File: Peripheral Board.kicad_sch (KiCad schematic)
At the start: 29 parts, among them J1 JAE_SIM_Card_SF72S006, J10 Conn_01x13_Male, J11 Conn_01x16_Male, J2 524372472, J4 5024268012, U1 MPU-9250, U7 XC6206-2.8V, U8 RT9166-12GVL

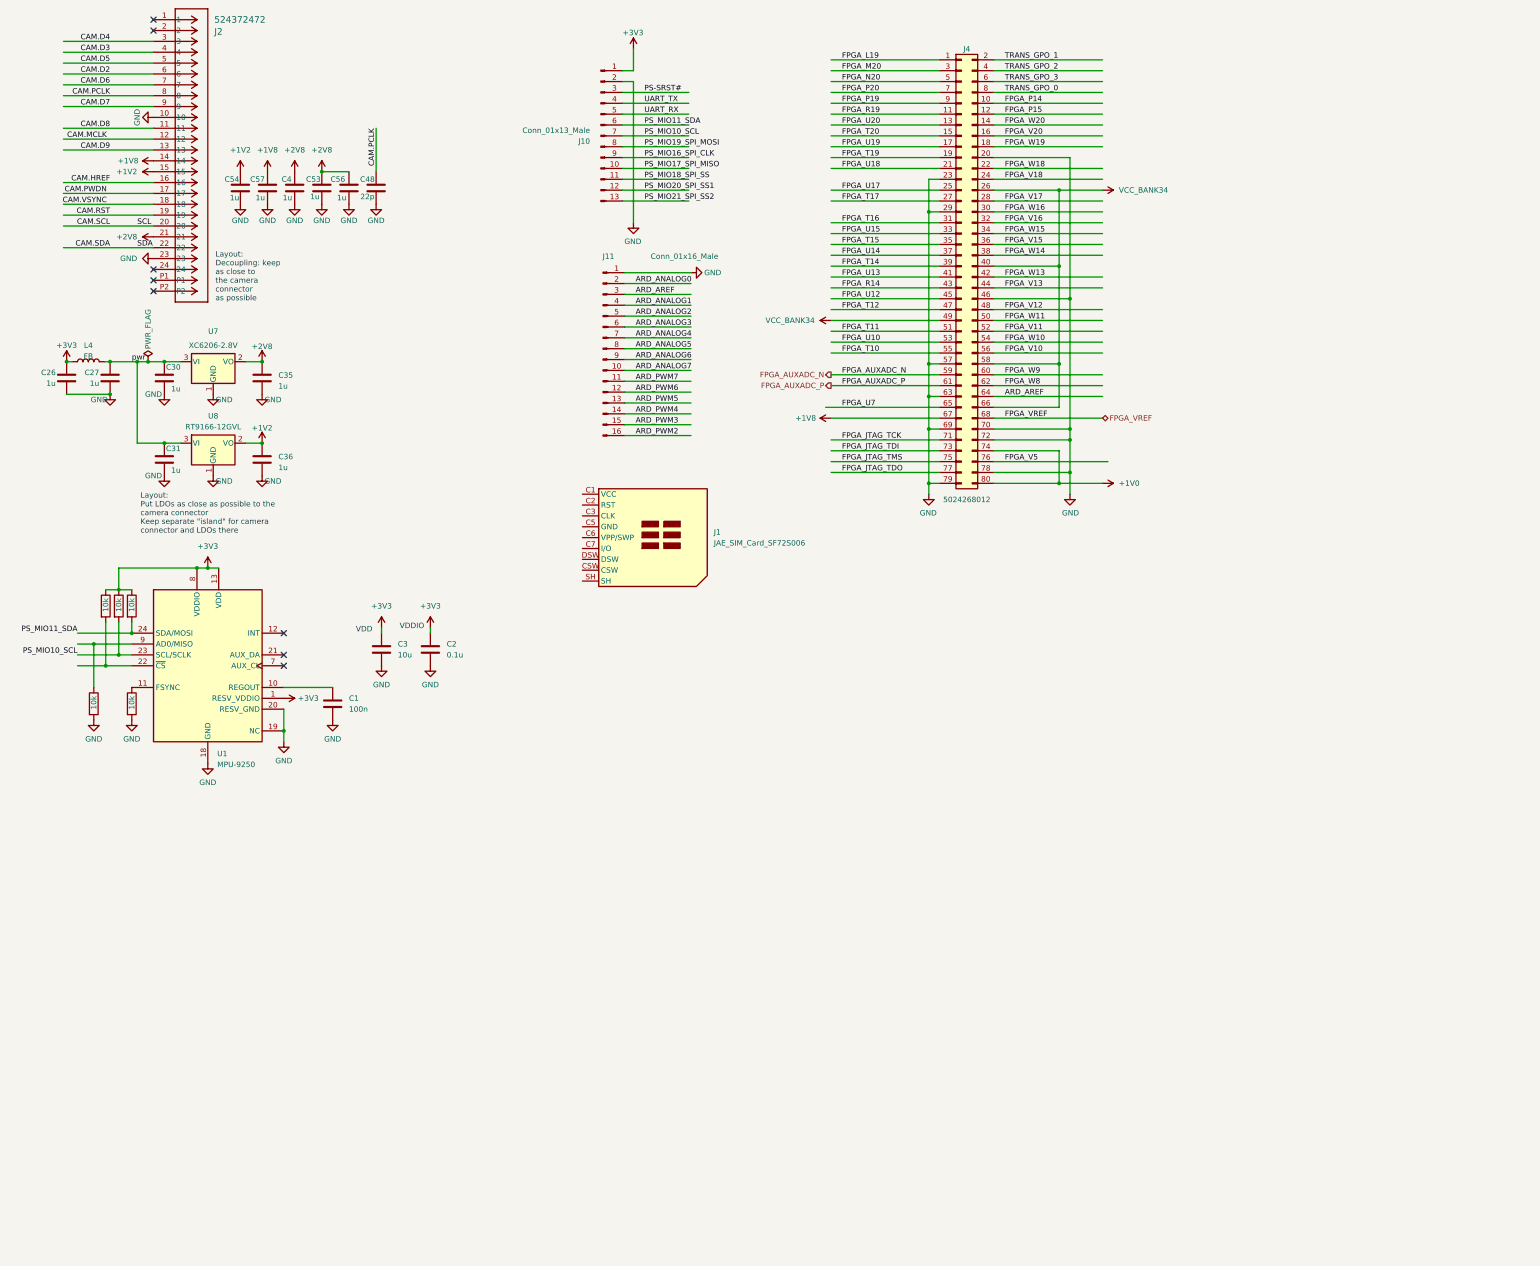
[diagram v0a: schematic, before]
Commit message: Added sd card, routed camera, and added esp32c3
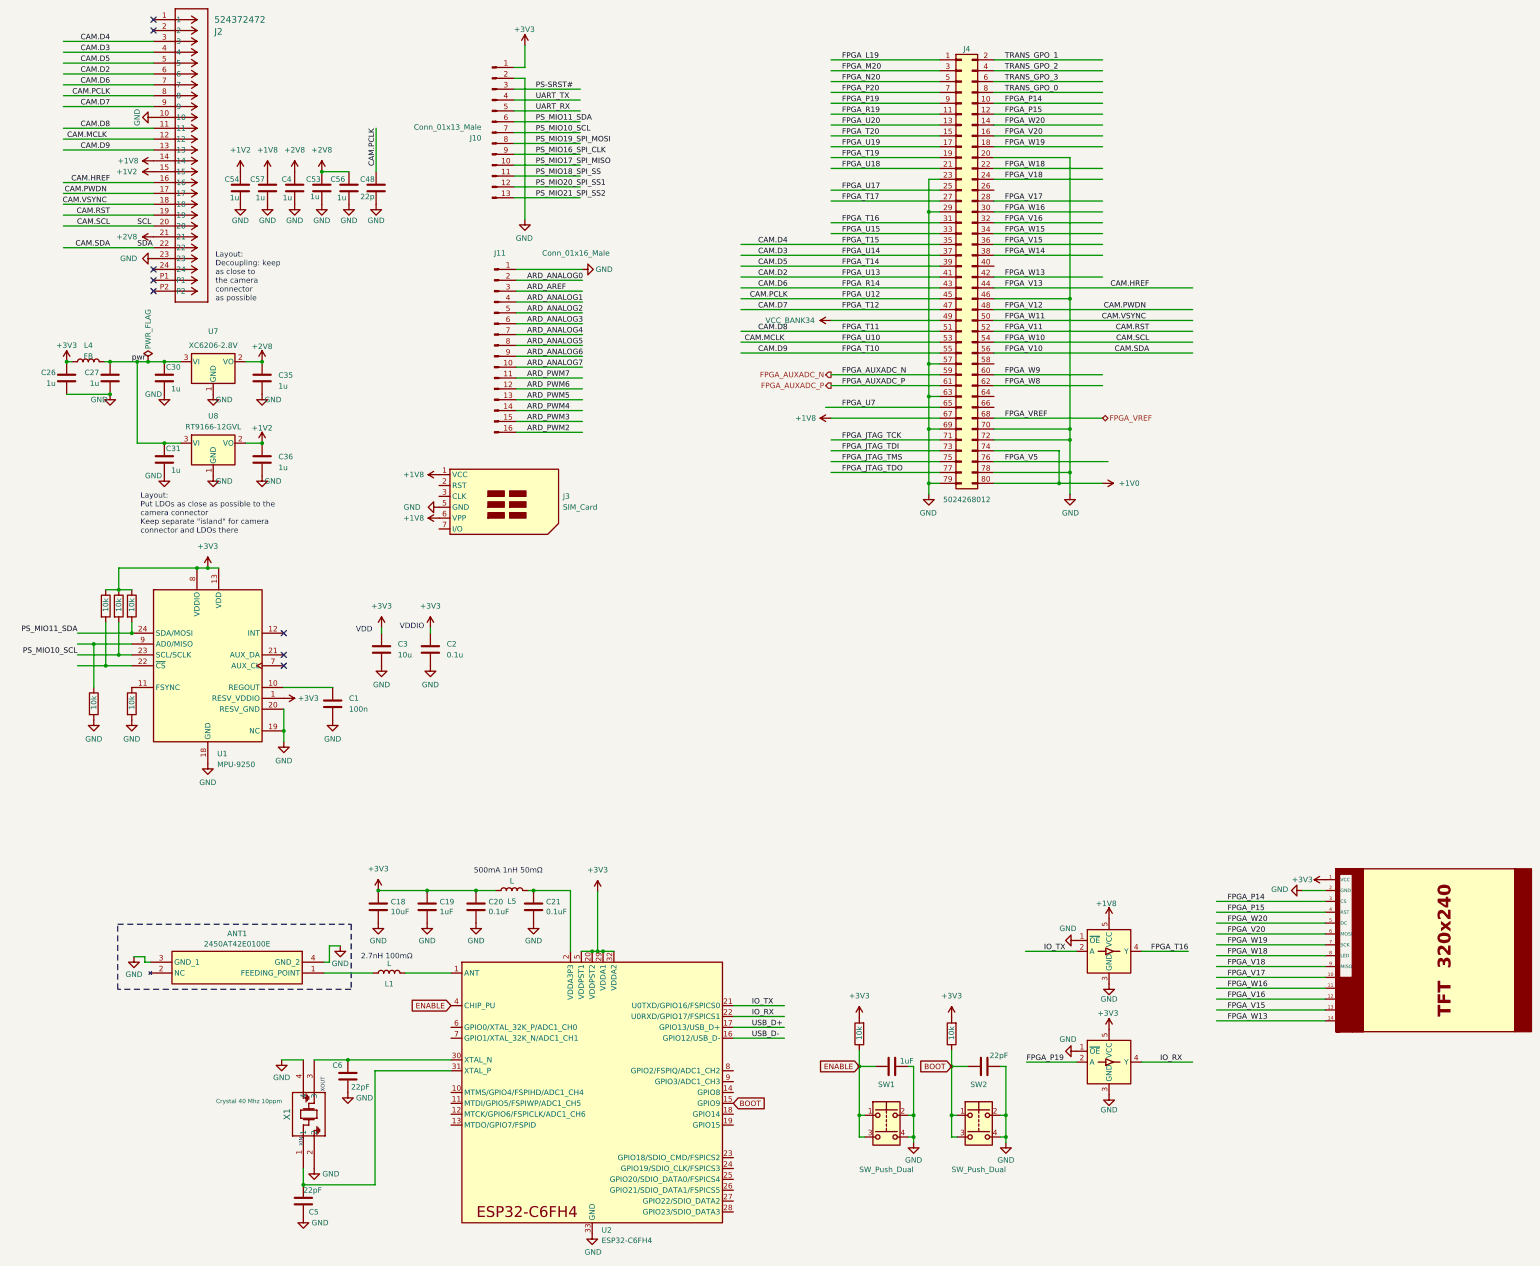
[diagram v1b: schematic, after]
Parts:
- removed J1: JAE_SIM_Card_SF72S006, Connector_JAE:JAE_SIM_Card_SF72S006, symbol Connector:JAE_SIM_Card_SF72S006
- added ANT1: 2450AT42E0100E, footprints:2450AT42E0100E-ANT, symbol Antenna:2450AT42E0100E
- added C18: 10uF, Capacitor_SMD:C_0402_1005Metric, symbol Device:C
- added C19, C7: 1uF, Capacitor_SMD:C_0402_1005Metric, symbol Device:C
- added C20, C21: 0.1uF, Capacitor_SMD:C_0402_1005Metric, symbol Device:C
- added C23, C5, C6: 22pF, Capacitor_SMD:C_0402_1005Metric, symbol Device:C
- added J3: SIM_Card, Connector_Card:nanoSIM_GCT_SIM8060-6-0-14-00, symbol Connector:SIM_Card
- added L1, L5: L, Inductor_SMD:L_0603_1608Metric, symbol Device:L
- added R18, R2: 10k, Resistor_SMD:R_0402_1005Metric, symbol Device:R
- added SW1, SW2: SW_Push_Dual, footprints:switch_SKSVCCE010, symbol Switch:SW_Push_Dual
- added U2: ESP32-C6FH4, Package_DFN_QFN:QFN-32-1EP_5x5mm_P0.5mm_EP3.6x3.6mm, symbol Espressif:ESP32-C6FH4
- added U3, U4: SN74LV1T125DBV, Package_TO_SOT_SMD:SOT-23-5, symbol Logic_LevelTranslator:SN74LV1T125DBV
- added U5: TFT_320x240, Library:TFT-320x240, symbol Z_Peripheral:TFT_320x240
- added X1: Crystal 40 Mhz 10ppm, footprints:Crystal_ECS-40Mhz_ECS, symbol Crystals:ECS-400-10-36B2-CKM-TR
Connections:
- net FPGA_R14 is gone; now on net CAM.D6: J4.43 (Pin_43)
- net FPGA_T10 is gone; now on net CAM.D9: J4.55 (Pin_55)
- net FPGA_T11 is gone; now on net CAM.D8: J4.51 (Pin_51)
- net FPGA_T12 is gone; now on net CAM.D7: J4.47 (Pin_47)
- net FPGA_T14 is gone; now on net CAM.D5: J4.39 (Pin_39)
- net FPGA_T15 is gone; now on net CAM.D4: J4.35 (Pin_35)
- net FPGA_U10 is gone; now on net CAM.MCLK: J4.53 (Pin_53)
- net FPGA_U12 is gone; now on net CAM.PCLK: J4.45 (Pin_45)
- net FPGA_U13 is gone; now on net CAM.D2: J4.41 (Pin_41)
- net FPGA_U14 is gone; now on net CAM.D3: J4.37 (Pin_37)
- net FPGA_V10 is gone; now on net CAM.SDA: J4.56 (Pin_56)
- net FPGA_V11 is gone; now on net CAM.RST: J4.52 (Pin_52)
- net FPGA_V12 is gone; now on net CAM.PWDN: J4.48 (Pin_48)
- net FPGA_V13 is gone; now on net CAM.HREF: J4.44 (Pin_44)
- net FPGA_W10 is gone; now on net CAM.SCL: J4.54 (Pin_54)
- net FPGA_W11 is gone; now on net CAM.VSYNC: J4.50 (Pin_50)
- net +1V8: now also J3.1 (VCC), J3.6 (VPP), U3.5 (VCC)
- net +3V3: now also C18.2, C19.2, C20.2, L5.1, R18.2, R2.2, U2.20 (VDDPST2), U2.29 (VDDA1), U2.32 (VDDA2), U2.5 (VDDPST1), U4.5 (VCC), U5.1 (VCC)
- net ARD_AREF: no longer J4.64 (Pin_64)
- net FPGA_P14: now also U5.3 (CS)
- net FPGA_P15: now also U5.4 (RST)
- net FPGA_P19: now also U4.2 (A)
- net FPGA_T16: now also U3.4 (Y)
- net FPGA_V15: now also U5.13
- net FPGA_V16: now also U5.12
- net FPGA_V17: now also U5.10
- net FPGA_V18: now also U5.9 (MISO)
- net FPGA_V20: now also U5.6 (MOSI)
- net FPGA_W13: now also U5.14
- net FPGA_W16: now also U5.11
- net FPGA_W18: now also U5.8 (LED)
- net FPGA_W19: now also U5.7 (SCK)
- net FPGA_W20: now also U5.5 (DC)
- net GND: now also ANT1.3 (GND_1), ANT1.4 (GND_2), C18.1, C19.1, C20.1, C21.1, C23.2, C5.1, C6.2, C7.1, J3.5 (GND), SW1.2, SW1.4, SW2.2, SW2.4, U2.33 (GND), U3.1 (~{OE}), U3.3 (GND), U4.1 (~{OE}), U4.3 (GND), U5.2 (GND), X1.2, X1.4
- net VCC_BANK34: no longer J4.26 (Pin_26), J4.40 (Pin_40), J4.58 (Pin_58), J4.66 (Pin_66)
- new net: ANT1.1 (FEEDING_POINT), L1.1
- new net: L1.2, U2.1 (ANT)
- new net: C21.2, L5.2, U2.2 (VDDA3P3), U2.3 (VDDA3P3)
- new net: C6.1, U2.30 (XTAL_N), X1.3
- new net: C5.2, U2.31 (XTAL_P), X1.1
- new net BOOT: C23.1, R18.1, SW2.1, SW2.3, U2.15 (GPIO9)
- new net ENABLE: C7.2, R2.1, SW1.1, SW1.3, U2.4 (CHIP_PU)
- new net IO_RX: U2.22 (U0RXD/GPIO17/FSPICS1), U4.4 (Y)
- new net IO_TX: U2.21 (U0TXD/GPIO16/FSPICS0), U3.2 (A)
- new net USB_D+: U2.17 (GPIO13/USB_D+)
- new net USB_D-: U2.16 (GPIO12/USB_D-)
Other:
- note added: "2.7nH 100mΩ"
- note added: "500mA 1nH 50mΩ"
- note added: "XIN"
- note added: "XOUT"
- moved on the sheet: J10, J11
